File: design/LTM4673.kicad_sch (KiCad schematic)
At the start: 96 parts, among them U35 LTM4673IY#PBF

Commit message: LTM4673.kicad_sch: remove 13 incorrect Footprint attributes
The ones that are kept match Marble.kicad_pcb.
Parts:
- C127: footprint CAPMP7343X310N -> Capacitor_Tantalum_SMD:CP_EIA-7343-30_AVX-N
- C140, C144, C148, C150, C151, C152: footprint CAPC1608X87N -> Capacitors SMD:CAPC1005X55N
- C195, C330, C341, C345: footprint CAPC3216X180N -> CAPC3225X270N
- C346, C347: footprint CAPC2012X135N -> CAPC1608X87N
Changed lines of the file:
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@@
       (effects (font (size 1.27 1.27)) (justify left bottom) hide)
     )
-    (property "Footprint" "CAPC1608X87N" (id 7) (at 54.102 226.822 0)
-      (effects (font (size 1.27 1.27)) (justify left bottom) hide)
-    )
     (property "Pin Count" "2" (id 8) (at 54.102 226.822 0)
       (effects (font (size 1.27 1.27)) (justify left bottom) hide)
@@
       (effects (font (size 1.27 1.27)) (justify left bottom) hide)
     )
-    (property "Footprint" "CAPC2012X135N" (id 7) (at 240.284 144.272 0)
-      (effects (font (size 1.27 1.27)) (justify left bottom) hide)
-    )
     (property "Pin Count" "2" (id 8) (at 240.284 144.272 0)
       (effects (font (size 1.27 1.27)) (justify left bottom) hide)
@@
       (effects (font (size 1.27 1.27)) (justify left bottom) hide)
     )
-    (property "Footprint" "CAPC1608X87N" (id 7) (at 62.484 182.372 0)
-      (effects (font (size 1.27 1.27)) (justify left bottom) hide)
-    )
     (property "Pin Count" "2" (id 8) (at 62.484 182.372 0)
       (effects (font (size 1.27 1.27)) (justify left bottom) hide)
@@
       (effects (font (size 1.27 1.27)) (justify left bottom) hide)
     )
-    (property "Footprint" "CAPC3216X180N" (id 7) (at 230.124 37.592 0)
-      (effects (font (size 1.27 1.27)) (justify left bottom) hide)
-    )
     (property "Pin Count" "2" (id 8) (at 230.124 37.592 0)
       (effects (font (size 1.27 1.27)) (justify left bottom) hide)
@@
       (effects (font (size 1.27 1.27)) (justify left bottom) hide)
     )
-    (property "Footprint" "CAPC1608X87N" (id 7) (at 56.642 167.894 0)
-      (effects (font (size 1.27 1.27)) (justify left bottom) hide)
-    )
     (property "Pin Count" "2" (id 8) (at 56.642 167.894 0)
       (effects (font (size 1.27 1.27)) (justify left bottom) hide)
@@
       (effects (font (size 1.27 1.27)) (justify left bottom) hide)
     )
-    (property "Footprint" "CAPC1608X87N" (id 7) (at 54.102 203.962 0)
-      (effects (font (size 1.27 1.27)) (justify left bottom) hide)
-    )
     (property "Pin Count" "2" (id 8) (at 54.102 203.962 0)
       (effects (font (size 1.27 1.27)) (justify left bottom) hide)
@@
       (effects (font (size 1.27 1.27)) (justify left bottom) hide)
     )
-    (property "Footprint" "CAPC3216X180N" (id 7) (at 230.124 195.072 0)
-      (effects (font (size 1.27 1.27)) (justify left bottom) hide)
-    )
     (property "Pin Count" "2" (id 8) (at 230.124 195.072 0)
       (effects (font (size 1.27 1.27)) (justify left bottom) hide)
@@
       (effects (font (size 1.27 1.27)) (justify left bottom) hide)
     )
-    (property "Footprint" "CAPC2012X135N" (id 7) (at 240.284 98.552 0)
-      (effects (font (size 1.27 1.27)) (justify left bottom) hide)
-    )
     (property "Pin Count" "2" (id 8) (at 240.284 98.552 0)
       (effects (font (size 1.27 1.27)) (justify left bottom) hide)
@@
       (effects (font (size 1.27 1.27)) (justify left bottom) hide)
     )
-    (property "Footprint" "CAPC3216X180N" (id 7) (at 237.744 195.072 0)
-      (effects (font (size 1.27 1.27)) (justify left bottom) hide)
-    )
     (property "Pin Count" "2" (id 8) (at 237.744 195.072 0)
       (effects (font (size 1.27 1.27)) (justify left bottom) hide)
@@
       (effects (font (size 1.27 1.27)) (justify left bottom) hide)
     )
-    (property "Footprint" "CAPC1608X87N" (id 7) (at 54.102 211.582 0)
-      (effects (font (size 1.27 1.27)) (justify left bottom) hide)
-    )
     (property "Pin Count" "2" (id 8) (at 54.102 211.582 0)
       (effects (font (size 1.27 1.27)) (justify left bottom) hide)
@@
       (effects (font (size 1.27 1.27)) (justify left bottom) hide)
     )
-    (property "Footprint" "CAPC1608X87N" (id 7) (at 62.484 192.532 0)
-      (effects (font (size 1.27 1.27)) (justify left bottom) hide)
-    )
     (property "Pin Count" "2" (id 8) (at 62.484 192.532 0)
       (effects (font (size 1.27 1.27)) (justify left bottom) hide)
@@
       (effects (font (size 1.27 1.27)) (justify left bottom) hide)
     )
-    (property "Footprint" "CAPC3216X180N" (id 7) (at 237.744 37.592 0)
-      (effects (font (size 1.27 1.27)) (justify left bottom) hide)
-    )
     (property "Pin Count" "2" (id 8) (at 237.744 37.592 0)
       (effects (font (size 1.27 1.27)) (justify left bottom) hide)
@@
       (effects (font (size 1.27 1.27)) (justify left bottom) hide)
     )
-    (property "Footprint" "CAPMP7343X310N" (id 7) (at 26.924 162.052 0)
-      (effects (font (size 1.27 1.27)) (justify left bottom) hide)
-    )

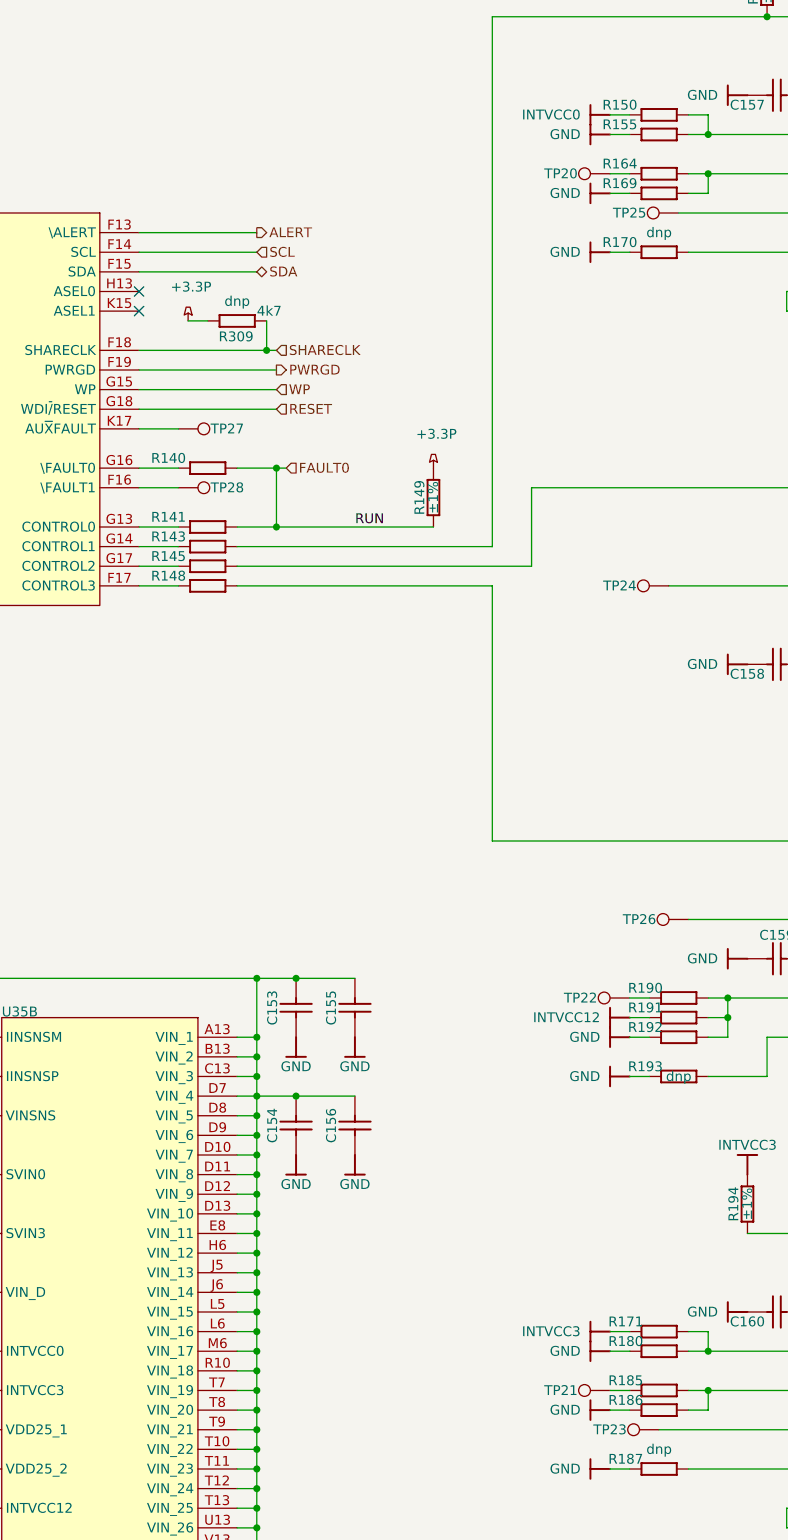
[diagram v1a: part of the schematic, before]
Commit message: external clock connected to power supply IC, PCB routing
external clock connected to power supply IC, PCB routing
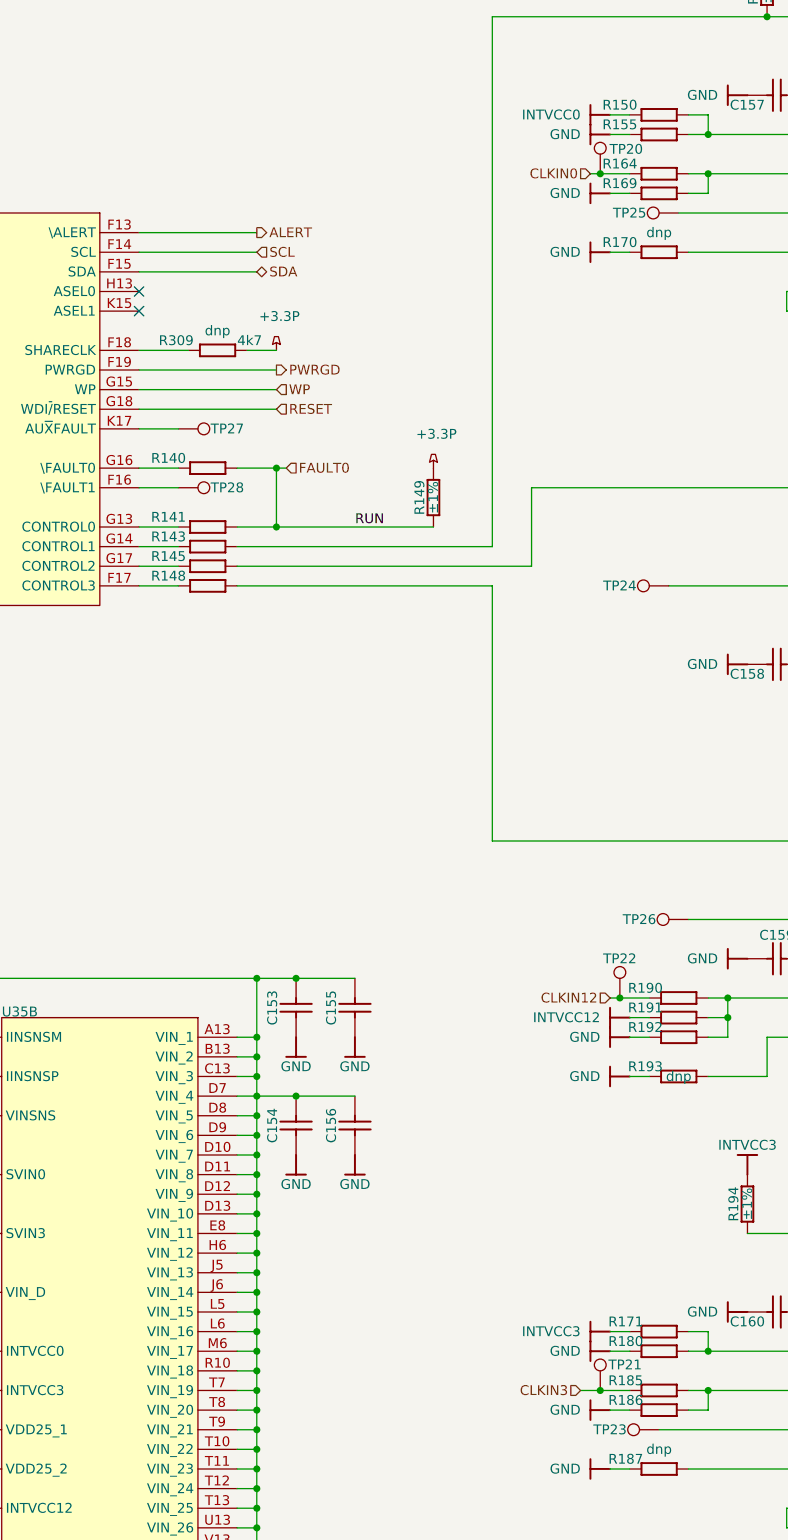
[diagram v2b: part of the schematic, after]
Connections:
- net +3.3P: now also R309.2; no longer R309.1
- net CLKIN0: now reaches R164.1, TP20.1
- net CLKIN3: now reaches R185.1, TP21.1
- net CLKIN12: now reaches R190.1, TP22.1
- net SHARECLK: no longer names the net of U35.F18 (SHARECLK)
- net SHARECLK: now also R309.1; no longer R309.2
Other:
- moved on the sheet: R309, TP20, TP21, TP22

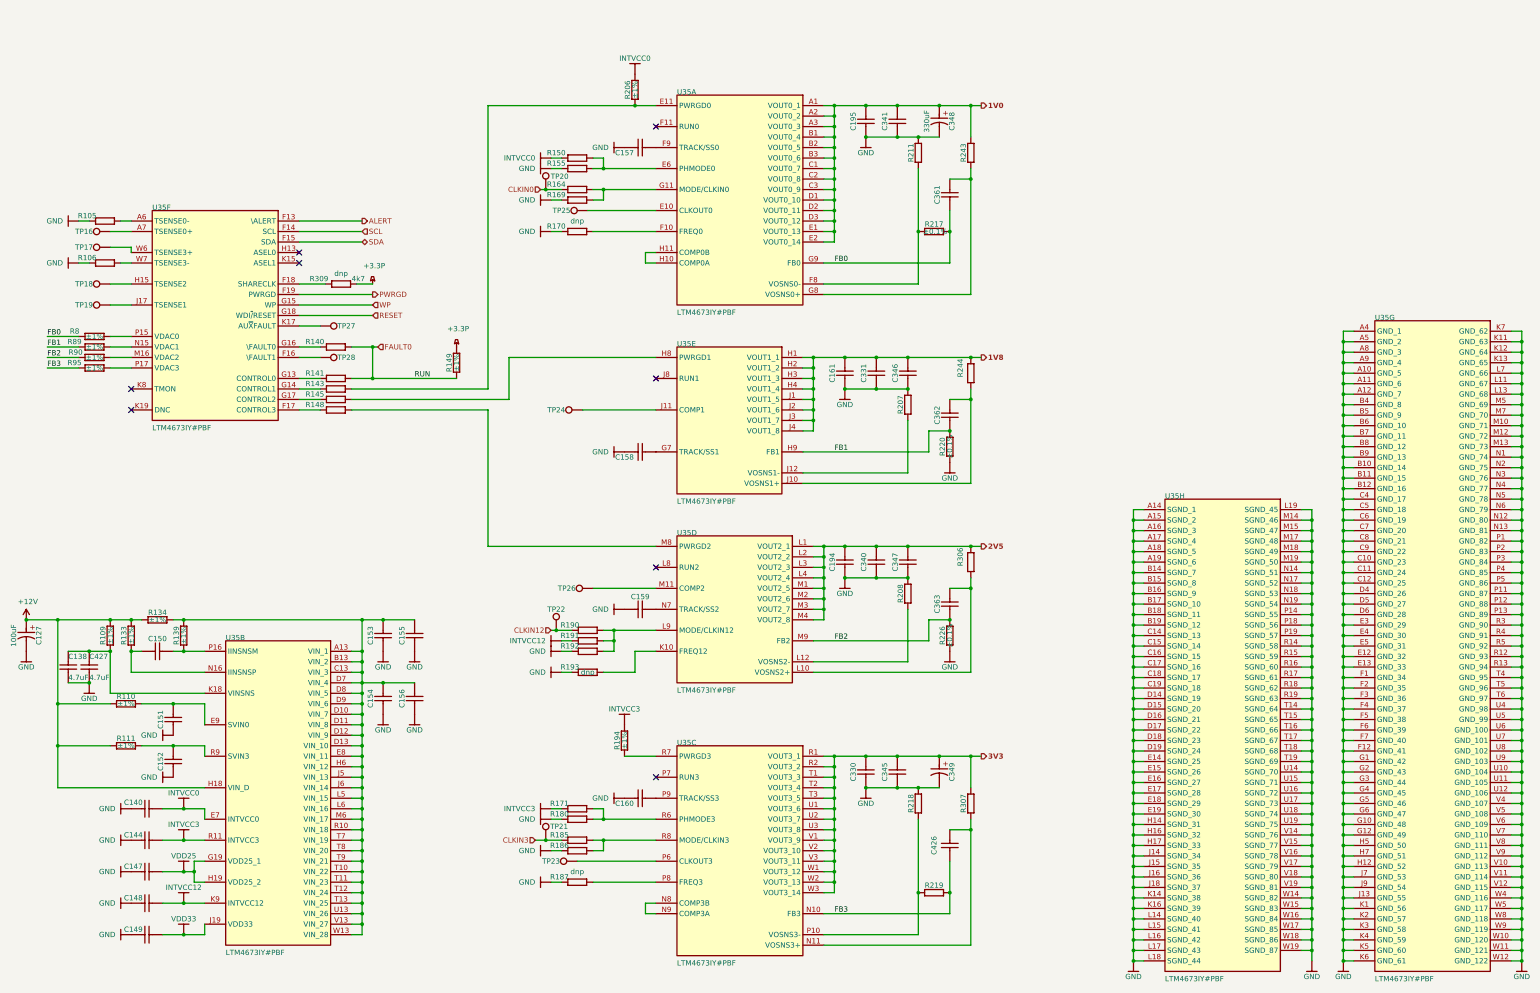
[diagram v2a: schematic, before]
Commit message: resistors r_DAC changed to 560k, R217 and R226 -> 0603, PCB routing
resistors r_DAC changed to 560k, R217 and R226 -> 0603, PCB routing
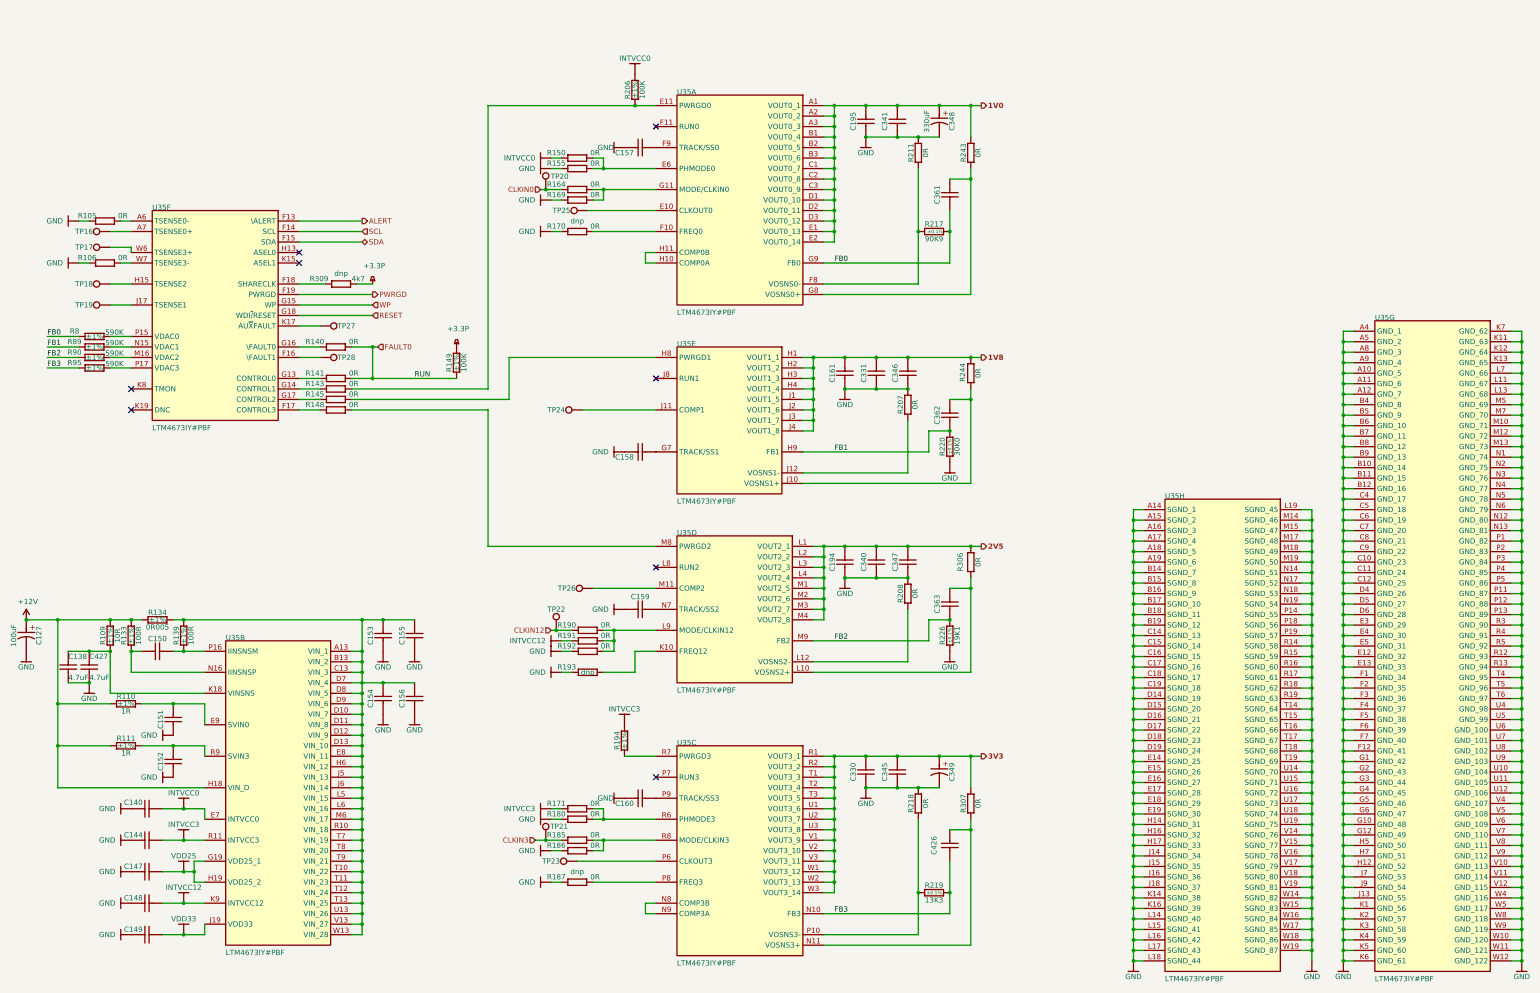
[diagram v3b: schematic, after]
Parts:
- R105, R106, R140, R141, R143, R145, R148, R150, R155, R164, R169, R170, R171, R180, R185, R186, R187, R190, R191, R192, R207, R208, R211, R218, R243, R244, R306, R307: value R0402_0R_JUMPER -> 0R
- R109: value R0402_10R_1%_0.0625W_200PPM -> 10R
- R110, R111: value R0402_1R_1%_0.0625W_200PPM -> 1R
- R133, R139: value R0402_100R_1%_0.1W_100PPM -> 100R
- R134: value R1206_0R005_1%_1.5W_75PPM_KOA_TLR2BP -> 0R005
- R149, R206: value R0402_100K_1%_0.0625W_100PPM -> 100K
- R217: value R0402_90K9_0.1%_0.063W_25PPM -> 90K9; footprint RESC1005X40N -> Resistors_SMD:RESC1608X55N; Manufacturer Part Number R0402_90K9_0.1%_0.063W_25PPM -> ERJ-PB3B9092V; Manufacturer1 Part Number ERA2AEB9092X -> ERJ-PB3B9092V
- R219: value R0603_13K3_0.1%_0.063W_10PPM -> 13K3; Manufacturer Part Number R0603_13K3_0.1%_0.063W_10PPM -> ERJ-PB3B1332V; Manufacturer1 Part Number RN73C1J13K3BTDF -> ERJ-PB3B1332V
- R220: value R0603_30K1_0.1%_0.063W_10PPM -> 30K0; Manufacturer Part Number R0603_30K1_0.1%_0.063W_10PPM -> ERJ-PB3B3002V; Manufacturer1 Part Number RN73C1J30K1BTDF -> ERJ-PB3B3002V; Part Number R0603_30K1_0.1%_0.063W_10PPM -> R0603_30K0_0.1%_0.063W_10PPM
- R226: value R0402_19K1_0.1%_0.063W_25PPM -> 19K1; footprint RESC1005X35N -> Resistors_SMD:RESC1608X55N; Manufacturer Part Number R0402_19K1_0.1%_0.063W_25PPM -> R0603_19K1_0.1%_0.063W_25PPM; Manufacturer1 Part Number CPF0402B19K1E1 -> ERJ-PB3B1912V; Part Number R0402_19K1_0.1%_0.063W_25PPM -> ERJ-PB3B1912V
- R8: value R0402_715k_1%_0.0625W_100PPM -> 590K; Author CERN DEM JLC -> CERN DEM BC; CreateDate 03.12.2007 -> 17.11.2020; LatestRevisionDate 17.10.2012 -> 17.11.2020; Manufacturer Part Number R0402_715k_1%_0.0625W_100PPM -> R0402_590K_1%_0.063W_100PPM; Manufacturer1 Example YAGEO PHYCOMP -> VISHAY; Manufacturer1 Part Number (none) -> CRCW0402590KFK; Part Number R0402_715k_1%_0.0625W_100PPM -> R0402_590K_1%_0.063W_100PPM; Power 0.0625W -> 0.063W; Status Not Recommended -> None
- R89: value R0402_402k_1%_0.0625W_100PPM -> 590K; Author CERN DEM JLC -> CERN DEM BC; CreateDate 03.12.2007 -> 17.11.2020; LatestRevisionDate 17.10.2012 -> 17.11.2020; Manufacturer Part Number R0402_402k_1%_0.0625W_100PPM -> R0402_590K_1%_0.063W_100PPM; Manufacturer1 Example YAGEO PHYCOMP -> VISHAY; Manufacturer1 Part Number (none) -> CRCW0402590KFK; Part Number R0402_402k_1%_0.0625W_100PPM -> R0402_590K_1%_0.063W_100PPM; Power 0.0625W -> 0.063W; Status Not Recommended -> None
- R90: value R0402_180K_1%_0.0625W_100PPM -> 590K; Author CERN DEM JLC -> CERN DEM BC; CreateDate 03.12.2007 -> 17.11.2020; LatestRevisionDate 17.10.2012 -> 17.11.2020; Manufacturer Part Number R0402_180K_1%_0.0625W_100PPM -> R0402_590K_1%_0.063W_100PPM; Manufacturer1 Example YAGEO PHYCOMP -> VISHAY; Manufacturer1 Part Number 232270671804L -> CRCW0402590KFK; Part Number R0402_180K_1%_0.0625W_100PPM -> R0402_590K_1%_0.063W_100PPM; Power 0.0625W -> 0.063W; Status Not Recommended -> None
- R95: value R0402_590K_1%_0.063W_100PPM -> 590K
